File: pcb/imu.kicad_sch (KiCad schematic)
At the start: 3 parts, among them U3 LM75ADP

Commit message: add top level schem and cleanup
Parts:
- removed C18: 0.1u, symbol Device:C
- removed R7: 4.7k, symbol Device:R
- removed U3: LM75ADP, symbol Sensor_Temperature:LM75B
- added C15: 0.1u, Capacitor_SMD:C_0402_1005Metric, symbol Device:C
- added C16: 2.2u, Capacitor_SMD:C_0402_1005Metric, symbol Device:C
- added C17: 10n, Capacitor_SMD:C_0402_1005Metric, symbol Device:C
- added U3: (no value), symbol IMU:ICM-42605
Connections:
- net +3.3V: now also C15.1, C16.1, C17.1, U3.12 (CS), U3.5 (VDDIO), U3.8 (VDD)
- net GND: now also C15.2, C16.2, C17.2, U3.6 (GND)
- net I2C.SCL: now also U3.13 (SCL)
- net I2C.SDA: now also U3.14 (SDA)
- no-connect marks 1 -> 7
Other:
- note added: "I2C IMU"
- note removed: "10/27/26"
- note removed: "LM75ADP Schematic"
- note removed: "Rev 1"
- note removed: "Topher Fontana"
- title: (none) -> IMU Sensor

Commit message: cleanup routing
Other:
- moved on the sheet: C15, C16, C17, U3

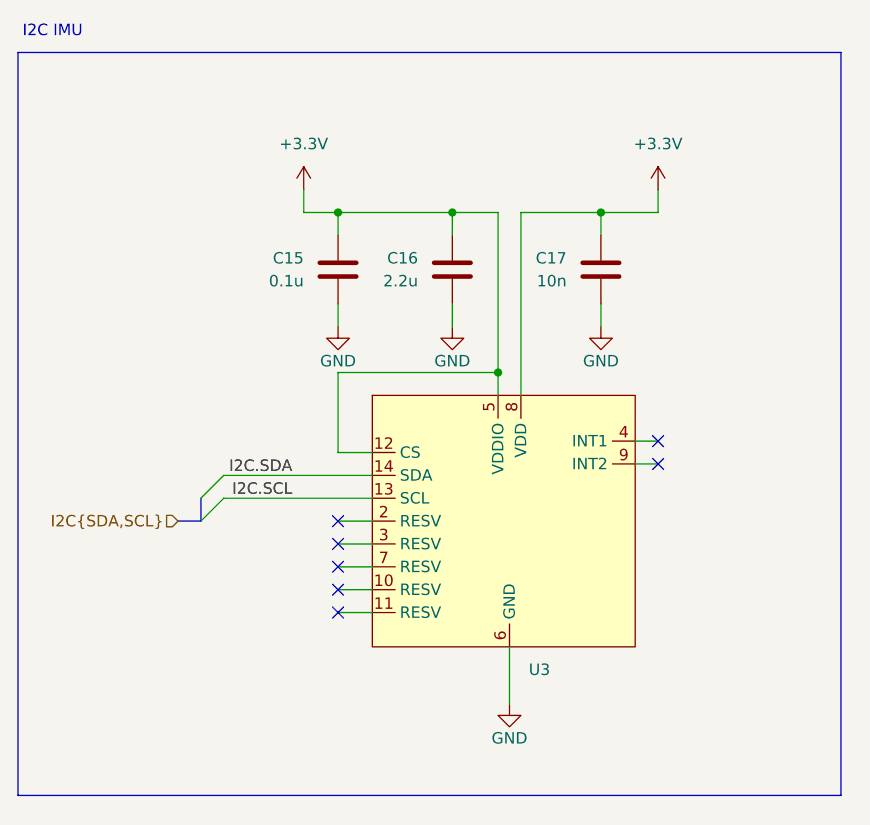
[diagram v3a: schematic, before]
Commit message: custom symbols for all ics
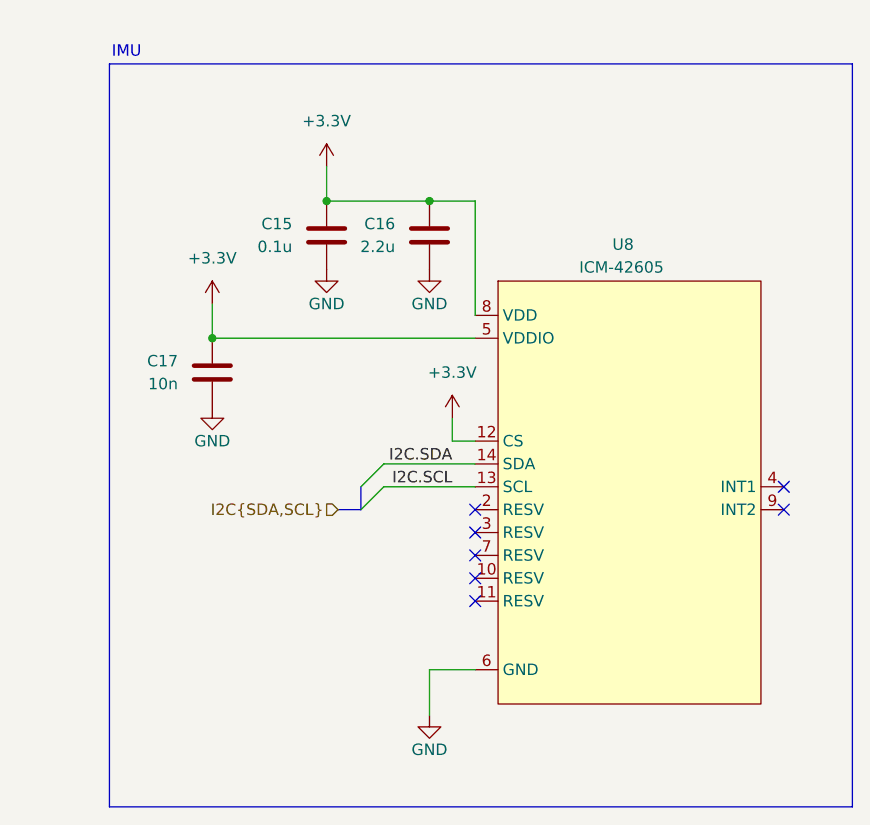
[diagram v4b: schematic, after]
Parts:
- removed U3: (no value), symbol IMU:ICM-42605
- added U8: ICM-42605, symbol IMU:ICM-42605
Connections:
- net +3.3V: now also U8.12 (CS), U8.5 (VDDIO), U8.8 (VDD)
- net GND: now also U8.6 (GND)
- net I2C.SCL: now also U8.13 (SCL)
- net I2C.SDA: now also U8.14 (SDA)
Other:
- note added: "IMU"
- note removed: "I2C IMU"
- moved on the sheet: C15, C16, C17

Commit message: Adding docs for GPIO and Color and removing INT
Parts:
- U8: Manufactuer PN (none) -> 1428-1152-2-ND; Vendor (none) -> Digikey; Vendor PN (none) -> 1428-1152-2-ND
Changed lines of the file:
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@@
 	(title_block
 		(title "IMU Sensor")
-		(date "2026-10-27")
+		(date "2026-10-28")
+		(rev "2")
 	)
 	(rectangle
@@
 			(width 0)
 			(type default)
+		)
+	)
+	(table
+		(column_count 2)
+		(border
+			(external yes)
+			(header yes)
+			(stroke
+				(width 0)
+				(type solid)
+			)
+		)
+		(separators
+			(rows yes)
+			(cols yes)
+			(stroke
+				(width 0)
+				(type solid)
+			)
+		)
+		(column_widths 21.59 30.48)
+		(row_heights 2.54 2.54 2.54 2.54 2.54)
+		(cells
+			(table_cell "Device"
+				(exclude_from_sim no)
+				(at 190.5 97.79 0)
+				(size 21.59 2.54)
+				(margins 0.9525 0.9525 0.9525 0.9525)
+				(span 1 1)
+				(fill
+					(type none)
+				)
+				(effects
+					(font
+						(size 1.27 1.27)
+					)
+					(justify left top)
+				)
+			)
+			(table_cell "ICM-42605 (U8)"
+				(exclude_from_sim no)
+				(at 212.09 97.79 0)
+				(size 30.48 2.54)
+				(margins 0.9525 0.9525 0.9525 0.9525)
+				(span 1 1)
+				(fill
+					(type none)
+				)
+				(effects
+					(font
+						(size 1.27 1.27)
+					)
+					(justify left top)
+				)
+			)
+			(table_cell "Function"
+				(exclude_from_sim no)
+				(at 190.5 100.33 0)
+				(size 21.59 2.54)
+				(margins 0.9525 0.9525 0.9525 0.9525)
+				(span 1 1)
+				(fill
+					(type none)
+				)
+				(effects
+					(font
+						(size 1.27 1.27)
+					)
+					(justify left top)
+				)
+			)
+			(table_cell "Interial Measurement Unit\n"
+				(exclude_from_sim no)
+				(at 212.09 100.33 0)
+				(size 30.48 2.54)
+				(margins 0.9525 0.9525 0.9525 0.9525)
+				(span 1 1)
+				(fill
+					(type none)
+				)
+				(effects
+					(font
+						(size 1.27 1.27)
+					)
+					(justify left top)
+				)
+			)
+			(table_cell "I2C Address (7-bit)"
+				(exclude_from_sim no)
+				(at 190.5 102.87 0)
+				(size 21.59 2.54)
+				(margins 0.9525 0.9525 0.9525 0.9525)
+				(span 1 1)
+				(fill
+					(type none)
+				)
+				(effects
+					(font
+						(size 1.27 1.27)
+					)
+					(justify left top)
+				)
+			)
+			(table_cell "1101000 (0x68)"
+				(exclude_from_sim no)
+				(at 212.09 102.87 0)
+				(size 30.48 2.54)
+				(margins 0.9525 0.9525 0.9525 0.9525)
+				(span 1 1)
+				(fill
+					(type none)
+				)
+				(effects
+					(font
+						(size 1.27 1.27)
+					)
+					(justify left top)
+				)
+			)
+			(table_cell "Address Config"
+				(exclude_from_sim no)
+				(at 190.5 105.41 0)
+				(size 21.59 2.54)
+				(margins 0.9525 0.9525 0.9525 0.9525)
+				(span 1 1)
+				(fill
+					(type none)
+				)
+				(effects
+					(font
+						(size 1.27 1.27)
+					)
+					(justify left top)
+				)
+			)
+			(table_cell "AD0 on GND"
+				(exclude_from_sim no)
+				(at 212.09 105.41 0)
+				(size 30.48 2.54)
+				(margins 0.9525 0.9525 0.9525 0.9525)
+				(span 1 1)
+				(fill
+					(type none)
+				)
+				(effects
+					(font
+						(size 1.27 1.27)
+					)
+					(justify left top)
+				)
+			)
+			(table_cell "Voltage Range"
+				(exclude_from_sim no)
+				(at 190.5 107.95 0)
+				(size 21.59 2.54)
+				(margins 0.9525 0.9525 0.9525 0.9525)
+				(span 1 1)
+				(fill
+					(type none)
+				)
+				(effects
+					(font
+						(size 1.27 1.27)
+					)
+					(justify left top)
+				)
+			)
+			(table_cell "1.7-3.6V"
+				(exclude_from_sim no)
+				(at 212.09 107.95 0)
+				(size 30.48 2.54)
+				(margins 0.9525 0.9525 0.9525 0.9525)
+				(span 1 1)
+				(fill
+					(type none)
+				)
+				(effects
+					(font
+						(size 1.27 1.27)
+					)
+					(justify left top)
+				)
+			)
 		)
 	)
@@
 		(dnp no)
 		(property "Reference" "U8"
-			(at 161.29 78.486 0)
+			(at 161.544 103.124 0)
 			(show_name no)
 			(do_not_autoplace no)
@@
 		)
 		(property "Value" "ICM-42605"
-			(at 162.306 81.026 0)
+			(at 162.56 105.664 0)
 			(show_name no)
 			(do_not_autoplace no)
@@
 			)
 		)
-		(property "Datasheet" ""
-			(at 162.56 106.68 0)
-			(hide yes)
-			(show_name no)
-			(do_not_autoplace no)
-			(effects
-				(font
-					(size 1.27 1.27)
-				)
-			)
-		)
-		(property "Description" ""
+		(property "Datasheet" "https://invensense.tdk.com/download-pdf/icm-42605-datasheet/"
+			(at 162.56 106.68 0)
+			(hide yes)
+			(show_name no)
+			(do_not_autoplace no)
+			(effects
+				(font
+					(size 1.27 1.27)
+				)
+			)
+		)
+		(property "Description" "IMU ACCEL/GYRO/TEMP I2C/SPI LGA"
 			(at 162.56 106.68 0)
 			(hide yes)
@@
 		(property "Manufaturer PIN" ""
 			(at 162.56 106.68 0)
-			(show_name no)
-			(do_not_autoplace no)
+			(hide yes)
+			(show_name no)
+			(do_not_autoplace no)
+			(effects
+				(font
+					(size 1.27 1.27)
+				)
+			)
+		)
+		(property "Manufactuer PN" "1428-1152-2-ND"
+			(at 162.56 106.68 0)
+			(hide yes)
+			(show_name no)
+			(do_not_autoplace no)
+			(effects
+				(font
+					(size 1.27 1.27)
+				)
+			)
+		)
+		(property "Vendor" "Digikey"
+			(at 162.56 106.68 0)
+			(hide yes)
+			(show_name no)
+			(do_not_autoplace no)
+			(effects
+				(font
+					(size 1.27 1.27)
+				)
+			)
+		)
+		(property "Vendor PN" "1428-1152-2-ND"
+			(at 162.56 106.68 0)
+			(hide yes)
+			(show_name no)
+			(do_not_autoplace no)

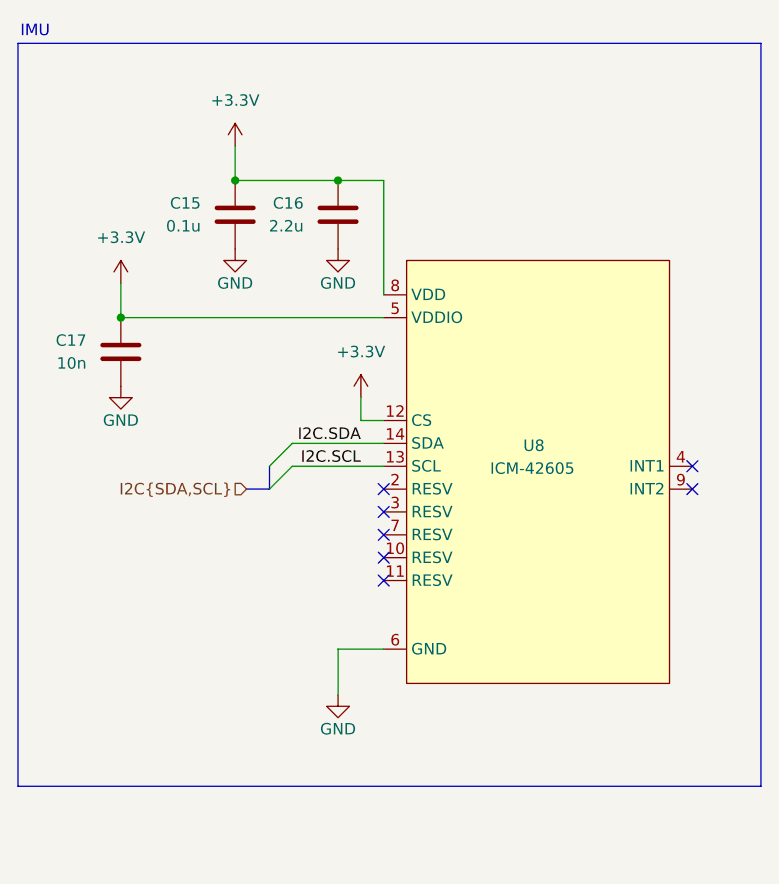
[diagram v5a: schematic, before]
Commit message: add AD0 to imu symbol
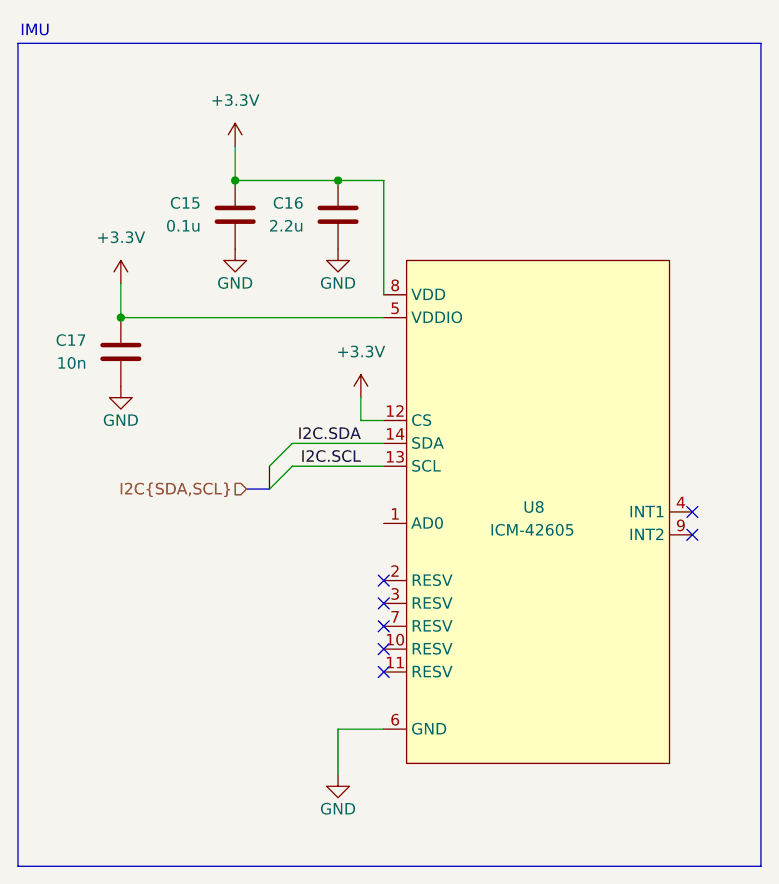
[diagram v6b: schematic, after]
